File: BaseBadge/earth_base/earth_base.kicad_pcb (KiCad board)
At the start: 2 copper layers, 57.5 x 18.5 mm, 9 parts, among them J1 Conn_02x03_Counter_Clockwise, J2 Conn_02x03_Counter_Clockwise

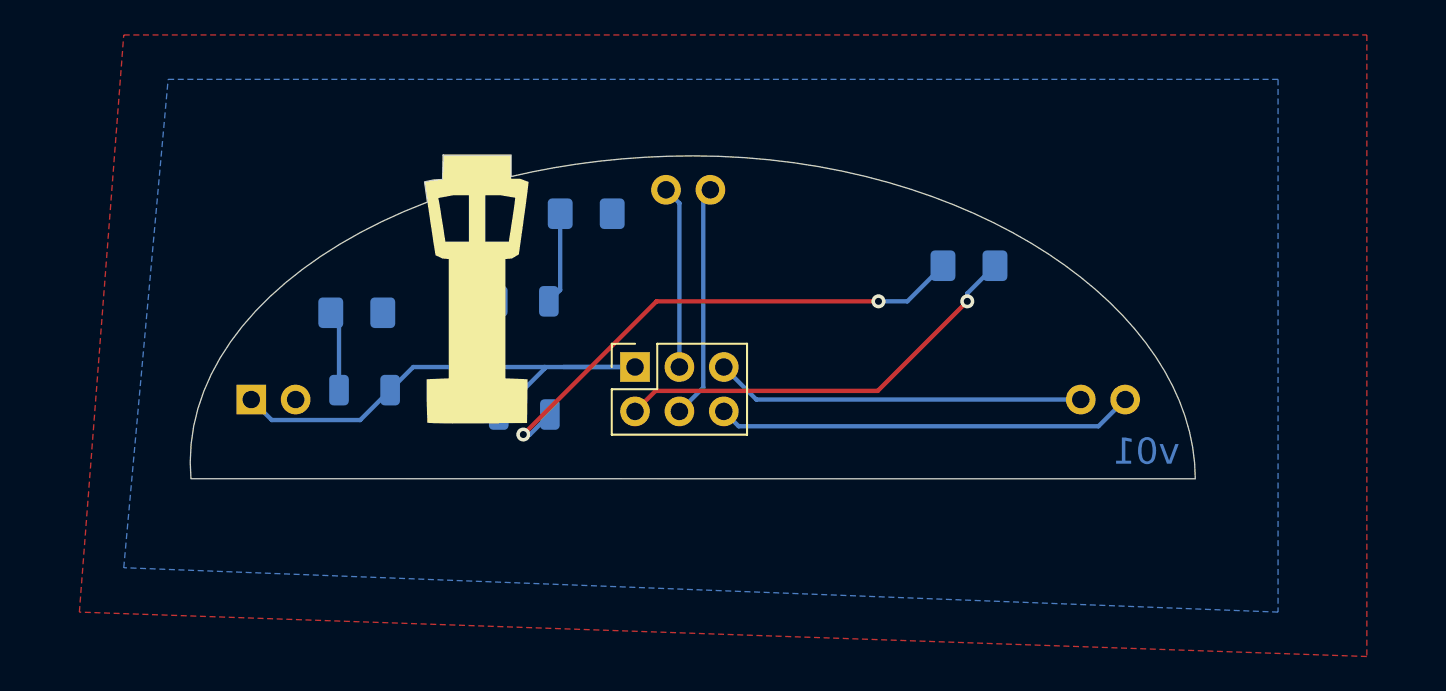
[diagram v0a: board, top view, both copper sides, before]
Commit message: updated earth portion for fabrication
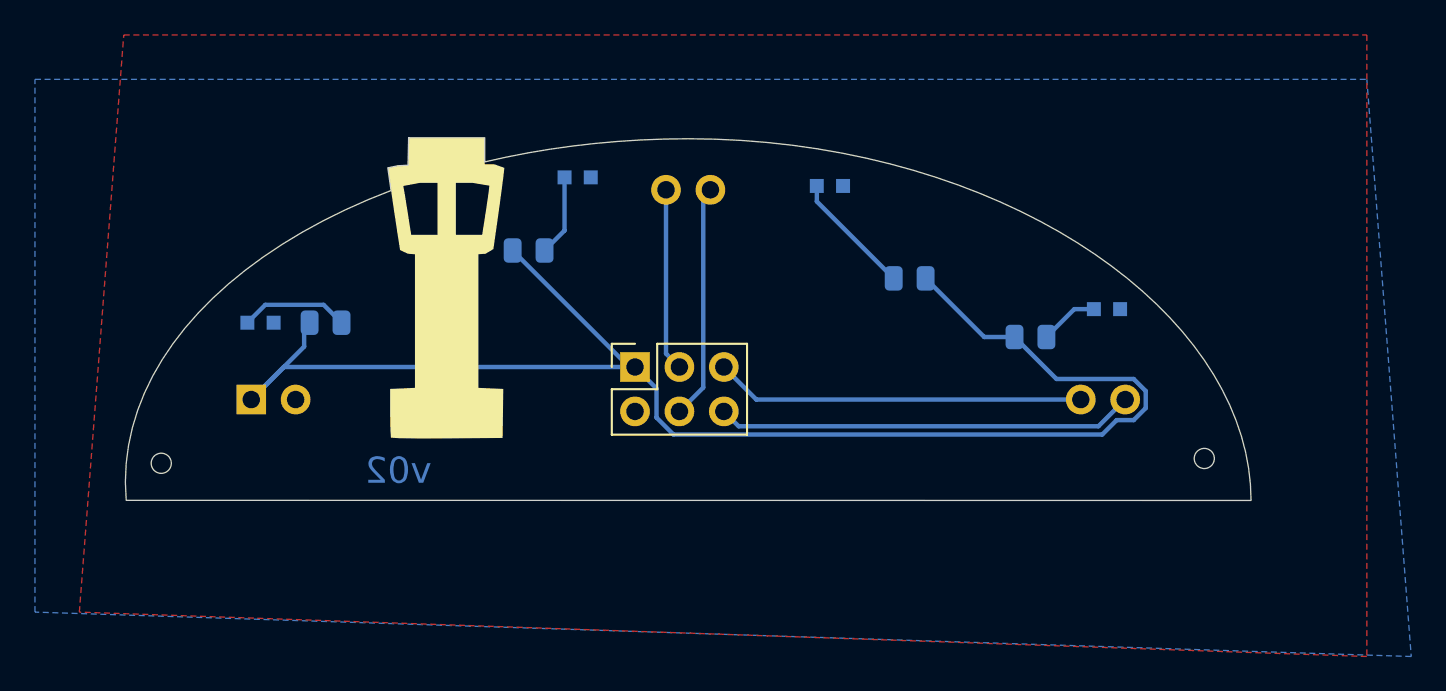
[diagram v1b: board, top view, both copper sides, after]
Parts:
- added D4: LED, Base_Library:19-213_Y2C-CO2R2L_3T(CY), B.Cu at (124.7, 102.8)
- added R4: 330, Resistor_SMD:R_0805_2012Metric, B.Cu at (128.4, 102.8)
- added REF**: SMT_Tooling_hole, aerospace_badge:SMT_Tooling_hole, F.Cu at (119.0, 110.9)
- added REF**: SMT_Tooling_hole, aerospace_badge:SMT_Tooling_hole, F.Cu at (178.7, 110.6)
- D1, D2, D3: footprint LED_SMD:LED_1206_3216Metric_Pad1.42x1.75mm_HandSolder -> Base_Library:19-213_Y2C-CO2R2L_3T(CY)
- R1, R2, R3: footprint Resistor_SMD:R_1206_3216Metric -> Resistor_SMD:R_0805_2012Metric
- moved R2 31.8 mm to (161.8, 100.3)
- moved R1 29.3 mm to (168.7, 103.6)
- moved D2 28.0 mm to (157.2, 95.0)
- moved D1 8.28 mm to (173.1, 102.0)
- moved R3 2.92 mm to (140.0, 98.7)
- moved svg2mod 2.86 mm to (147.8, 106.5)
- moved D3 2.14 mm to (142.8, 94.5)
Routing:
- net VCC: track 35.4 -> 86.9 mm
- net Net-(D1-Pad2): track 30.0 -> 3.37 mm, vias 2 -> 0
- net GND: track 24.3 -> 0.00 mm, vias 1 -> 0
- net Net-(D4-Pad2): track 0.00 -> 6.23 mm
- net Net-(D2-Pad2): track 4.62 -> 7.11 mm
- net Net-(D3-Pad2): track 5.28 -> 4.66 mm
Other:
- board size 57.5 x 18.5 mm -> 64.4 x 20.7 mm
- board text added: "v02"
- board text removed: "v01"

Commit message: updated per latest protoype discoveries
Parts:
- D1, D2, D3, D4: footprint Base_Library:19-213_Y2C-CO2R2L_3T(CY) -> aerospace_badge:NCD0805W2
- moved D4 6.89 mm to (130.3, 98.9)
- moved D3 3.09 mm to (139.8, 95.4)
- moved D1 0.84 mm to (172.2, 102.0)
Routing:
- net Net-(D4-Pad2): track 6.23 -> 3.99 mm
- net Net-(D1-Pad2): track 3.37 -> 2.35 mm
- net Net-(D3-Pad2): track 4.66 -> 4.14 mm
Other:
- board text added: "v03"
- board text removed: "v02"
